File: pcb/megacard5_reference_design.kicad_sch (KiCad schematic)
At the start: 24 parts, among them J1 MegaCard 5, J10 SMTSO2545CTJ, J11 S7B-PH-SM4-TB(LF)(SN), J12 S7B-PH-SM4-TB(LF)(SN), J13 SMTSO2545CTJ, J2 7V to 50V input, SW1 ~{POWER_OFF}, SW2 ~{EXT_RESET}, SW3 AFT

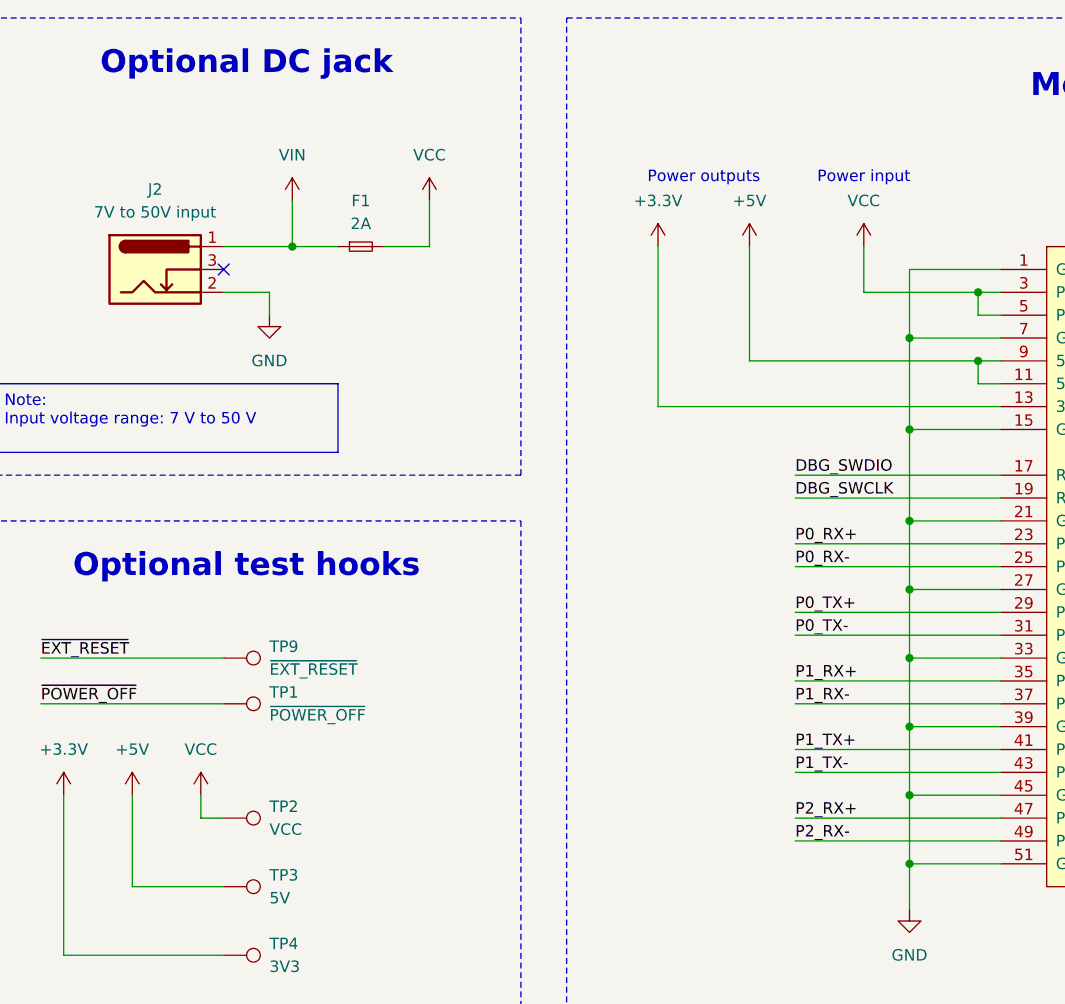
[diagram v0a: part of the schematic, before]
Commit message: renamed VCC to PWR_IN
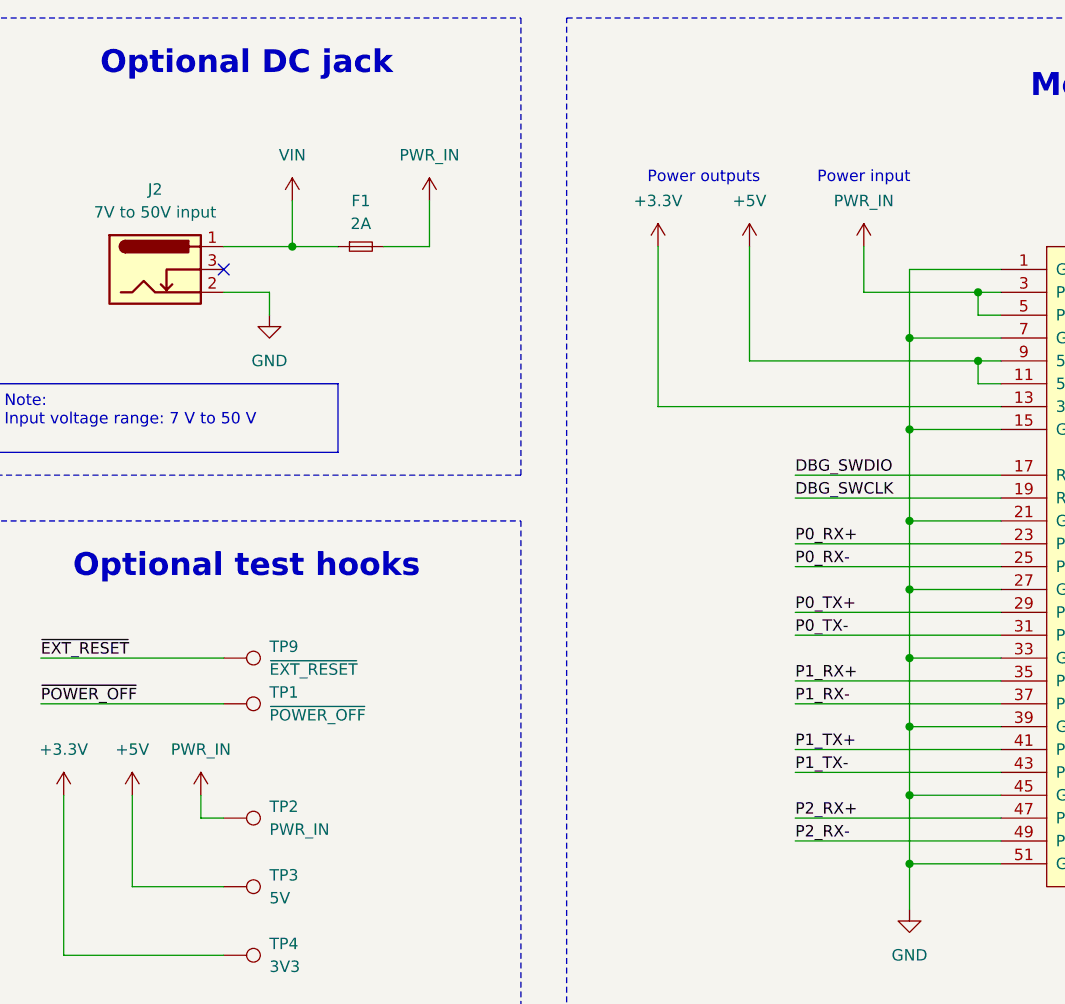
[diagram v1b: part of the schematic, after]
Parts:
- TP2: value VCC -> PWR_IN
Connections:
- net VCC renamed PWR_IN
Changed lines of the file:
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@@
 			)
 		)
-		(property "Value" "VCC"
+		(property "Value" "PWR_IN"
 			(at 124.46 45.72 0)
 			(effects
@@
 			)
 		)
-		(property "Value" "VCC"
+		(property "Value" "PWR_IN"
 			(at 50.8 106.68 0)
 			(effects
@@
 			)
 		)
-		(property "Value" "VCC"
+		(property "Value" "PWR_IN"
 			(at 76.2 40.64 0)
 			(effects
@@
 			)
 		)
-		(property "Value" "VCC"
+		(property "Value" "PWR_IN"
 			(at 58.42 115.5699 90)
 			(effects
